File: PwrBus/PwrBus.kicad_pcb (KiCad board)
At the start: 2 copper layers, 149.9 x 25.4 mm, 8 parts, among them J1 Screw_Terminal_01x02, J2 Screw_Terminal_01x02, J3 Screw_Terminal_01x02, J4 Screw_Terminal_01x02, J5 Screw_Terminal_01x02, J6 Screw_Terminal_01x02, J7 Screw_Terminal_01x02, Q1 IRLML5203

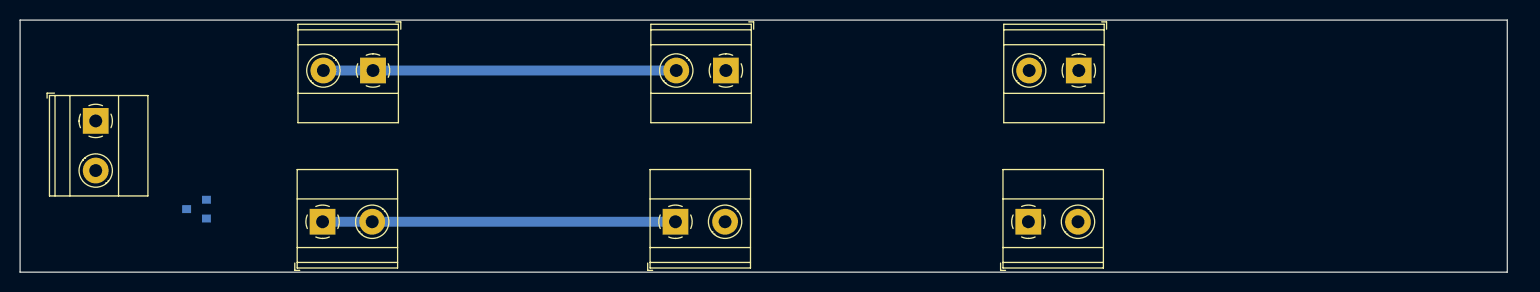
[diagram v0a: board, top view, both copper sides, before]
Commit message: Move sockets
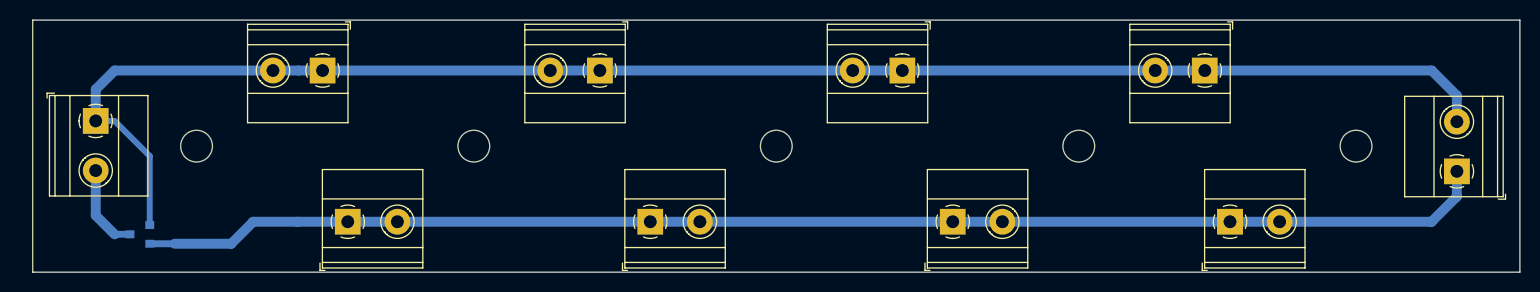
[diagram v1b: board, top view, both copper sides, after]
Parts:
- added H1: MountingHole, MountingHole:MountingHole_3.2mm_M3, F.Cu at (68.6, 63.5)
- added H2: MountingHole, MountingHole:MountingHole_3.2mm_M3, F.Cu at (96.5, 63.5)
- added H3: MountingHole, MountingHole:MountingHole_3.2mm_M3, F.Cu at (127.0, 63.5)
- added H4: MountingHole, MountingHole:MountingHole_3.2mm_M3, F.Cu at (157.5, 63.5)
- added H5: MountingHole, MountingHole:MountingHole_3.2mm_M3, F.Cu at (185.4, 63.5)
- added J10: Screw_Terminal_01x02, TerminalBlock_Phoenix:TerminalBlock_Phoenix_MKDS-1,5-2_1x02_P5.00mm_Horizontal, F.Cu at (195.6, 66.0)
- added J8: Screw_Terminal_01x02, TerminalBlock_Phoenix:TerminalBlock_Phoenix_MKDS-1,5-2_1x02_P5.00mm_Horizontal, F.Cu at (172.7, 71.1)
- added J9: Screw_Terminal_01x02, TerminalBlock_Phoenix:TerminalBlock_Phoenix_MKDS-1,5-2_1x02_P5.00mm_Horizontal, F.Cu at (170.2, 55.9)
- moved J7 17.8 mm to (139.7, 55.9)
- moved J5 12.7 mm to (109.2, 55.9)
- moved J6 7.62 mm to (144.8, 71.1)
- moved Q1 6.25 mm to (62.9, 72.4)
- moved J3 5.08 mm to (81.3, 55.9)
- moved J4 2.54 mm to (114.3, 71.1)
- moved J2 2.54 mm to (83.8, 71.1)
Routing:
- net GND: track 35.6 -> 158.6 mm
- net VCC: track 35.6 -> 136.1 mm
- net Net-(J1-Pad2): track 0.00 -> 8.76 mm

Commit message: Power bus is ready
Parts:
- added D1: LED, LED_THT:LED_D5.0mm, F.Cu at (36.8, 25.4)
- added R1: 1k, Resistor_SMD:R_0805_2012Metric_Pad1.20x1.40mm_HandSolder, B.Cu at (36.8, 32.1)
- moved J9 59.0 mm to (125.1, 17.8), turned to 0 degrees
- moved J5 59.0 mm to (64.1, 17.8), turned to 0 degrees
- moved J3 55.2 mm to (41.3, 17.8)
- moved J7 55.2 mm to (99.7, 17.8)
- moved H3 54.8 mm to (87.6, 25.4)
- moved J1 54.8 mm to (19.1, 22.9)
- moved J10 54.8 mm to (156.2, 27.9)
- moved Q1 54.8 mm to (23.5, 34.3)
- moved H1 54.8 mm to (29.2, 25.4)
- moved H2 54.8 mm to (57.1, 25.4)
- moved H4 54.8 mm to (118.1, 25.4)
- moved H5 54.8 mm to (146.1, 25.4)
- moved J4 54.3 mm to (75.6, 33.0)
- moved J8 54.3 mm to (134.0, 33.0)
- moved J6 50.8 mm to (111.1, 33.0), turned to 180 degrees
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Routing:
- net GND: track 158.6 -> 166.5 mm
- net Net-(D1-Pad2): track 0.00 -> 3.17 mm
- net VCC: track 136.1 -> 138.3 mm
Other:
- board text added: "+5V"
- board text added: "Gnd"

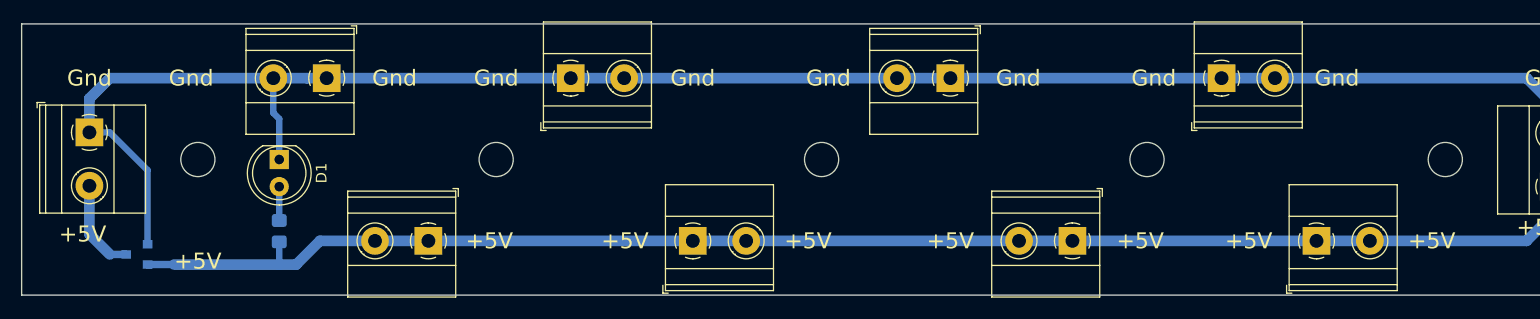
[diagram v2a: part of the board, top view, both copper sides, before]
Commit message: Polishing Power Bus
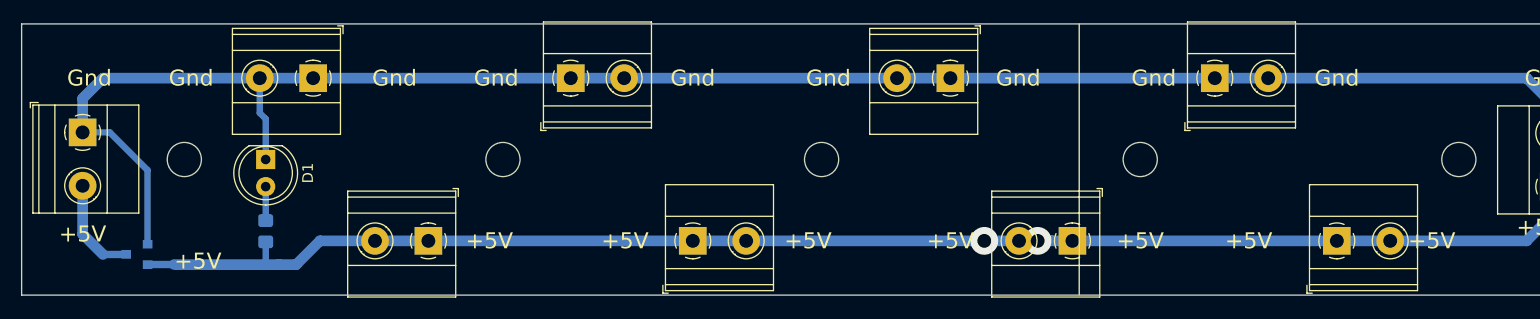
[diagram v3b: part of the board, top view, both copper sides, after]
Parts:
- moved J8 1.90 mm to (135.9, 33.0)
- moved H1 1.27 mm to (27.9, 25.4)
- moved D1 1.27 mm to (35.6, 25.4)
- moved J3 1.27 mm to (40.0, 17.8)
- moved R1 1.27 mm to (35.6, 32.1)
- moved H5 1.27 mm to (147.3, 25.4)
- moved H4 0.64 mm to (117.5, 25.4)
- moved J9 0.64 mm to (124.5, 17.8)
- moved J1 0.64 mm to (18.4, 22.9)
- moved H2 0.63 mm to (57.8, 25.4)
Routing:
- net GND: track 166.5 -> 167.8 mm
- net Net-(J1-Pad2): track 8.76 -> 9.39 mm
- net VCC: vias 0 -> 2
